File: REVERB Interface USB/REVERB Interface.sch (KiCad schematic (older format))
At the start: 60 parts, among them J1 RPiZeroW, J2 Iridium, J3 APRS, J4 Antenna, J6 USB_B_Micro, J7 USB, J8 USBPOGO, M1 MountingHole_Pad, M2 MountingHole_Pad, M3 MountingHole_Pad, M4 MountingHole_Pad, M5 PiMount, M6 PiMount, M7 PiMount, M8 PiMount, U1 LSM9DS1BOB, U2 MAX3232, U3 CY7C65213-28PVXI, U4 LD1117S33TR_SOT223

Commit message: Remove LDO
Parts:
- removed C10: 0.1uF, Capacitor_SMD:C_0805_2012Metric_Pad1.18x1.45mm_HandSolder, symbol Device:C
- removed C9: 4.7uF, Capacitor_SMD:C_0805_2012Metric_Pad1.18x1.45mm_HandSolder, symbol Device:C
- removed U4: LD1117S33TR_SOT223, Package_TO_SOT_SMD:SOT-223-3_TabPin2, symbol Regulator_Linear:LD1117S33TR_SOT223
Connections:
- net labels removed: SW7STEP3V3
- wire segments 110 -> 102
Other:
- note removed: "5V VCC for 5V USB logic level, 3V3 VCCIO for 3V3 UART output"
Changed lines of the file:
@@
 Text Label 3550 4600 0    50   ~ 0
 D-
-Text Label 2200 4000 0    50   ~ 0
-SW7STEP3V3
 $Comp
 L power:GND #PWR0123
@@
 	1    0    0    -1
 $EndComp
-Text Label 1250 6000 1    50   ~ 0
-SW7
 $Comp
 L power:GND #PWR0127
@@
 	1    0    0    -1
 $EndComp
-Text Label 1450 5200 0    50   ~ 0
-SW7
 Text Label 1450 5400 0    50   ~ 0
 D+
@@
 	3050 4000 3250 4000
 Text Label 3250 4000 0    50   ~ 0
-SW7
-Wire Wire Line
-	1950 6050 2150 6050
-Wire Wire Line
-	2150 6050 2150 6300
-Connection ~ 1950 6050
-Text Label 3200 6300 0    50   ~ 0
-SW7STEP3V3
-Text Notes 850  6950 0    50   ~ 0
-5V VCC for 5V USB logic level, 3V3 VCCIO for 3V3 UART output
+SW10
 Wire Notes Line
 	850  3900 850  6950
@@
 Wire Notes Line
 	3700 3900 3700 6950
-$Comp
-L Regulator_Linear:LD1117S33TR_SOT223 U4
-U 1 1 61636412
-P 2450 6300
-F 0 "U4" H 2450 6542 50  0000 C CNN
-F 1 "LD1117S33TR_SOT223" H 2450 6451 50  0000 C CNN
-F 2 "Package_TO_SOT_SMD:SOT-223-3_TabPin2" H 2450 6500 50  0001 C CNN
-F 3 "http://www.st.com/st-web-ui/static/active/en/resource/technical/document/datasheet/CD00000544.pdf" H 2550 6050 50  0001 C CNN
-	1    2450 6300
-	1    0    0    -1
-$EndComp
-Wire Wire Line
-	1950 6650 2450 6650
-Wire Wire Line
-	2450 6600 2450 6650
-Connection ~ 2450 6650
-$Comp
-L Device:C C10
-U 1 1 616D4D0F
-P 3200 6450
-F 0 "C10" H 3315 6496 50  0000 L CNN
-F 1 "0.1uF" H 3315 6405 50  0000 L CNN
-F 2 "Capacitor_SMD:C_0805_2012Metric_Pad1.18x1.45mm_HandSolder" H 3238 6300 50  0001 C CNN
-F 3 "~" H 3200 6450 50  0001 C CNN
-	1    3200 6450
-	1    0    0    -1
-$EndComp
-$Comp
-L Device:C C9
-U 1 1 616D4D15
-P 2750 6450
-F 0 "C9" H 2865 6496 50  0000 L CNN
-F 1 "4.7uF" H 2865 6405 50  0000 L CNN
-F 2 "Capacitor_SMD:C_0805_2012Metric_Pad1.18x1.45mm_HandSolder" H 2788 6300 50  0001 C CNN
-F 3 "~" H 2750 6450 50  0001 C CNN
-	1    2750 6450
-	1    0    0    -1
-$EndComp
-Wire Wire Line
-	3200 6650 3200 6600
-Wire Wire Line
-	2450 6650 2750 6650
-Wire Wire Line
-	2750 6600 2750 6650
-Connection ~ 2750 6650
-Wire Wire Line
-	2750 6650 3200 6650
-Wire Wire Line
-	2750 6300 3200 6300
 $Comp
 L Device:LED D9
@@
 Wire Wire Line
 	10150 2350 10350 2350
+Wire Wire Line
+	2950 4000 3050 4000
+Connection ~ 2950 4000
+Connection ~ 3050 4000
+Text Label 1250 6000 1    50   ~ 0
+SW10
+Text Label 1450 5200 0    50   ~ 0
+SW10
 $EndSCHEMATC

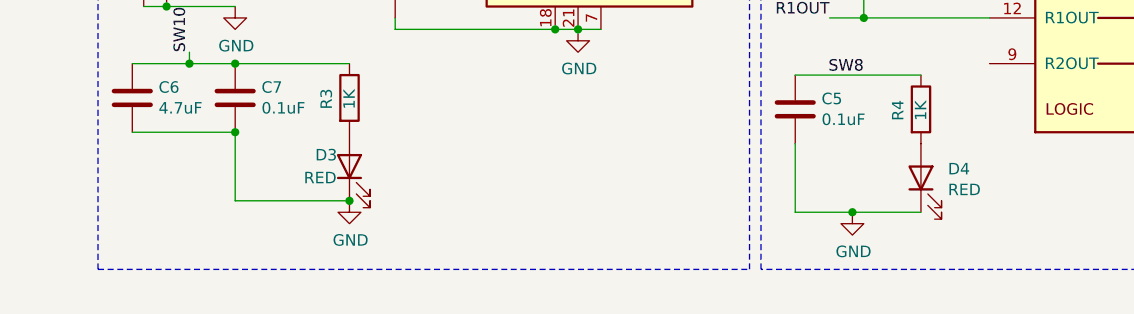
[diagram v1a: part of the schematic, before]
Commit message: Add note regarding usb programming
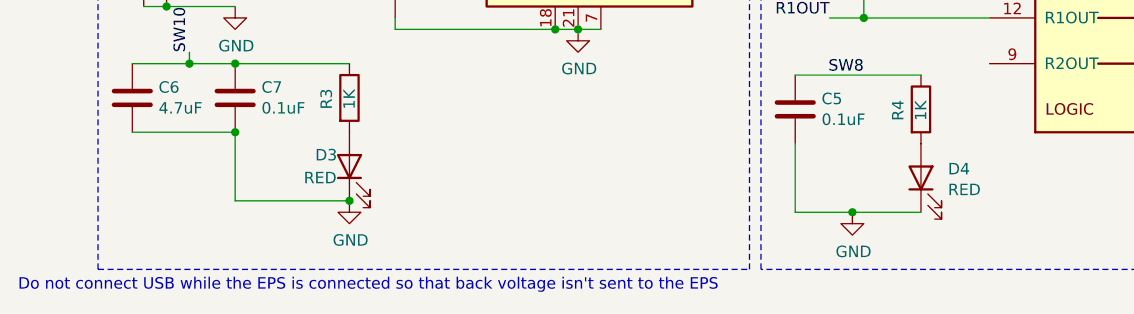
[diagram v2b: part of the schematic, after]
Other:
- note added: "Do not connect USB while the EPS is connected so that back voltage isn't sent to the EPS"
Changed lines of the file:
@@
 Text Label 1450 5200 0    50   ~ 0
 SW10
+Text Notes 500  7050 0    50   ~ 0
+Do not connect USB while the EPS is connected so that back voltage isn't sent to the EPS
 $EndSCHEMATC

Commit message: Replace max3232 footprint, update stencil
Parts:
- U2: footprint REVERB Interface:Texas_Instruments-MAX3232ID -> REVERB Interface:Texas_Instruments-MAX3232ID-Level_A
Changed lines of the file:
@@
 F 0 "U2" H 5550 6731 50  0000 C CNN
 F 1 "MAX3232" H 5550 6640 50  0000 C CNN
-F 2 "REVERB Interface:Texas_Instruments-MAX3232ID" H 5600 4300 50  0001 L CNN
+F 2 "REVERB Interface:Texas_Instruments-MAX3232ID-Level_A" H 5600 4300 50  0001 L CNN
 F 3 "https://datasheets.maximintegrated.com/en/ds/MAX3222-MAX3241.pdf" H 5550 5450 50  0001 C CNN
 	1    5550 5350
@@
 	10350 2350 10750 2350
 $Comp
-L power:GND #PWR?
+L power:GND #PWR0134
 U 1 1 6170EDA2
 P 10150 2350
-F 0 "#PWR?" H 10150 2100 50  0001 C CNN
+F 0 "#PWR0134" H 10150 2100 50  0001 C CNN
 F 1 "GND" H 10155 2177 50  0000 C CNN
 F 2 "" H 10150 2350 50  0001 C CNN

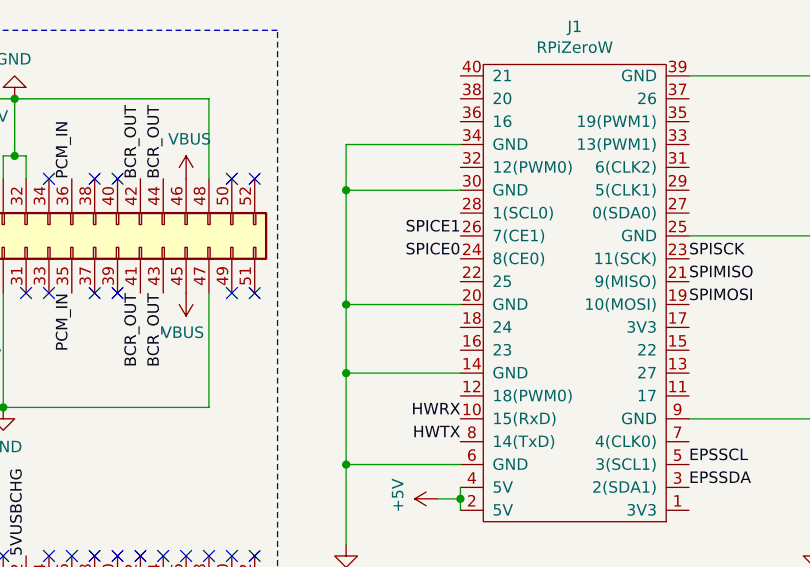
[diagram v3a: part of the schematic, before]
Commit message: Add bitbang uart connections
gpio 23 and 24, #2
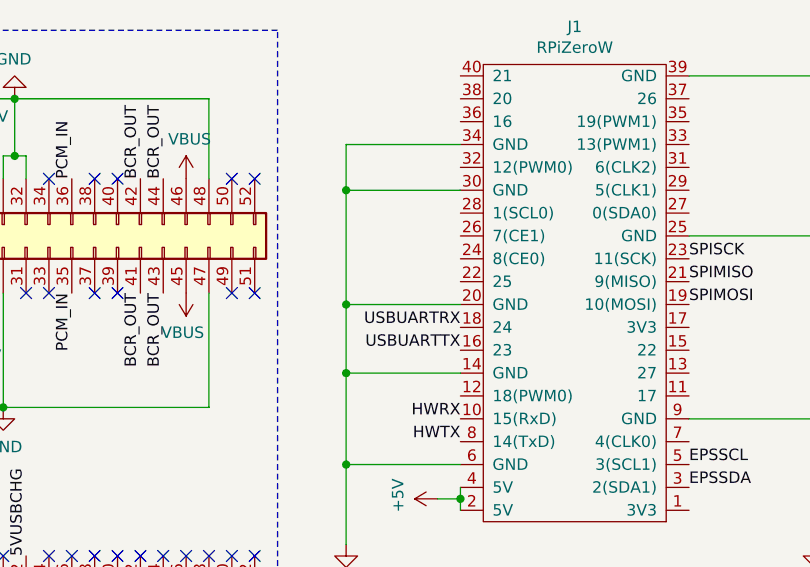
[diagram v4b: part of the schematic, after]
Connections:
- net USBUARTRX: now also J1.18 (24)
- net USBUARTTX: now also J1.16 (23)
- net SPICE0: no longer names the net of J1.24 (8(CE0))
- net SPICE1: no longer names the net of J1.26 (7(CE1))
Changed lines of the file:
@@
 Text Label 6100 1950 0    50   ~ 0
 SPIMOSI
-Text Label 5100 1650 2    50   ~ 0
-SPICE1
-Text Label 5100 1750 2    50   ~ 0
-SPICE0
 $Comp
 L Interface_USB:CY7C65213-28PVXI U3
@@
 Text Notes 500  7050 0    50   ~ 0
 Do not connect USB while the EPS is connected so that back voltage isn't sent to the EPS
+Text Label 5100 2050 2    50   ~ 0
+USBUARTRX
+Text Label 5100 2150 2    50   ~ 0
+USBUARTTX
 $EndSCHEMATC

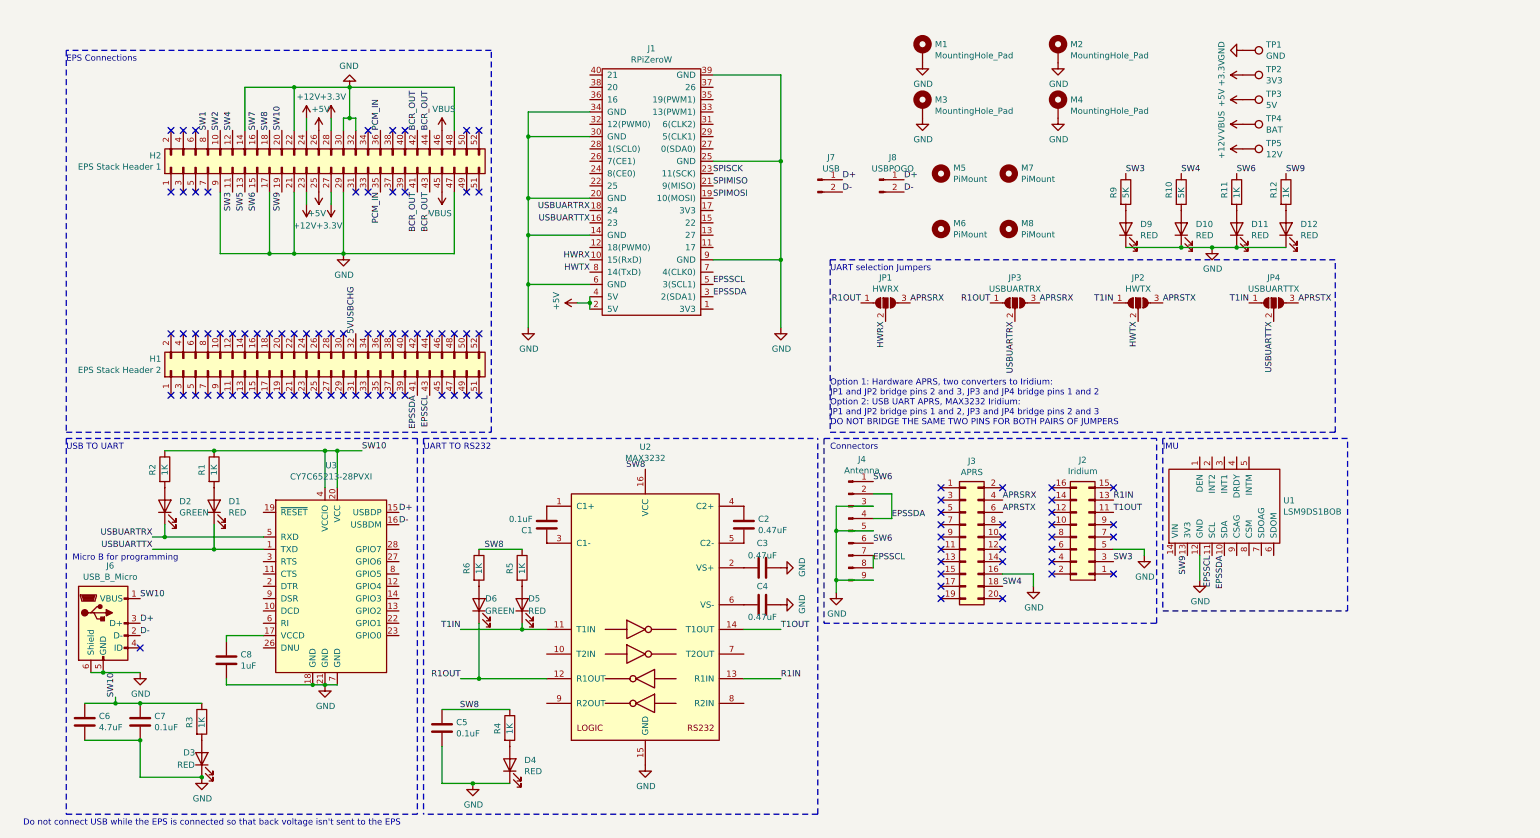
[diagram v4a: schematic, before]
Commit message: Add level shifters, updated sch revision numbers consistent with pcb
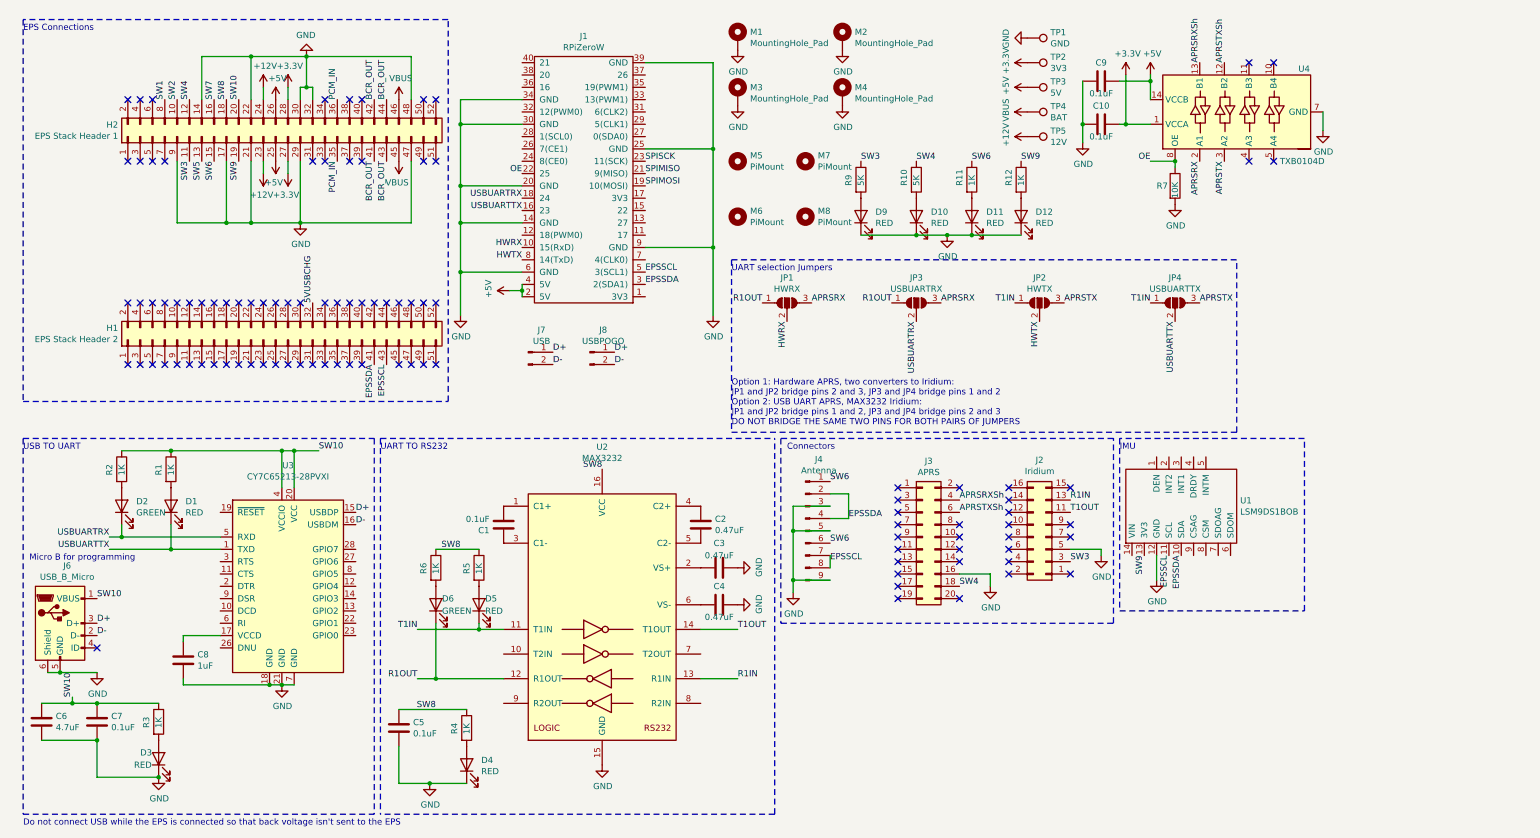
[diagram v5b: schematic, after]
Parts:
- added C10, C9: 0.1uF, Capacitor_SMD:C_0805_2012Metric_Pad1.18x1.45mm_HandSolder, symbol Device:C
- added R7: 10K, Resistor_SMD:R_0805_2012Metric_Pad1.20x1.40mm_HandSolder, symbol Device:R
- added U4: TXB0104D, Package_SO:SOIC-14_3.9x8.7mm_P1.27mm, symbol Logic_LevelTranslator:TXB0104D
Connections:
- net +3V3: now also C10.1, U4.1 (VCCA)
- net +5V: now also C9.1, U4.14 (VCCB)
- net APRSRX: now also U4.2 (A1); no longer J3.4 (Pin_4)
- net APRSTX: now also U4.3 (A2); no longer J3.6 (Pin_6)
- net GND: now also C10.2, C9.2, R7.2, U4.7 (GND)
- net OE: now reaches J1.22 (25)
- net OE: now also R7.1, U4.8 (OE)
- new net APRSRXSh: J3.4 (Pin_4), U4.13 (B1)
- new net APRSTXSh: J3.6 (Pin_6), U4.12 (B2)
- no-connect marks 96 -> 100
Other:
- moved on the sheet: C1, C2, C3, C4, C5, C6, C7, C8, D1, D10, D11, D12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

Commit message: tie OE high
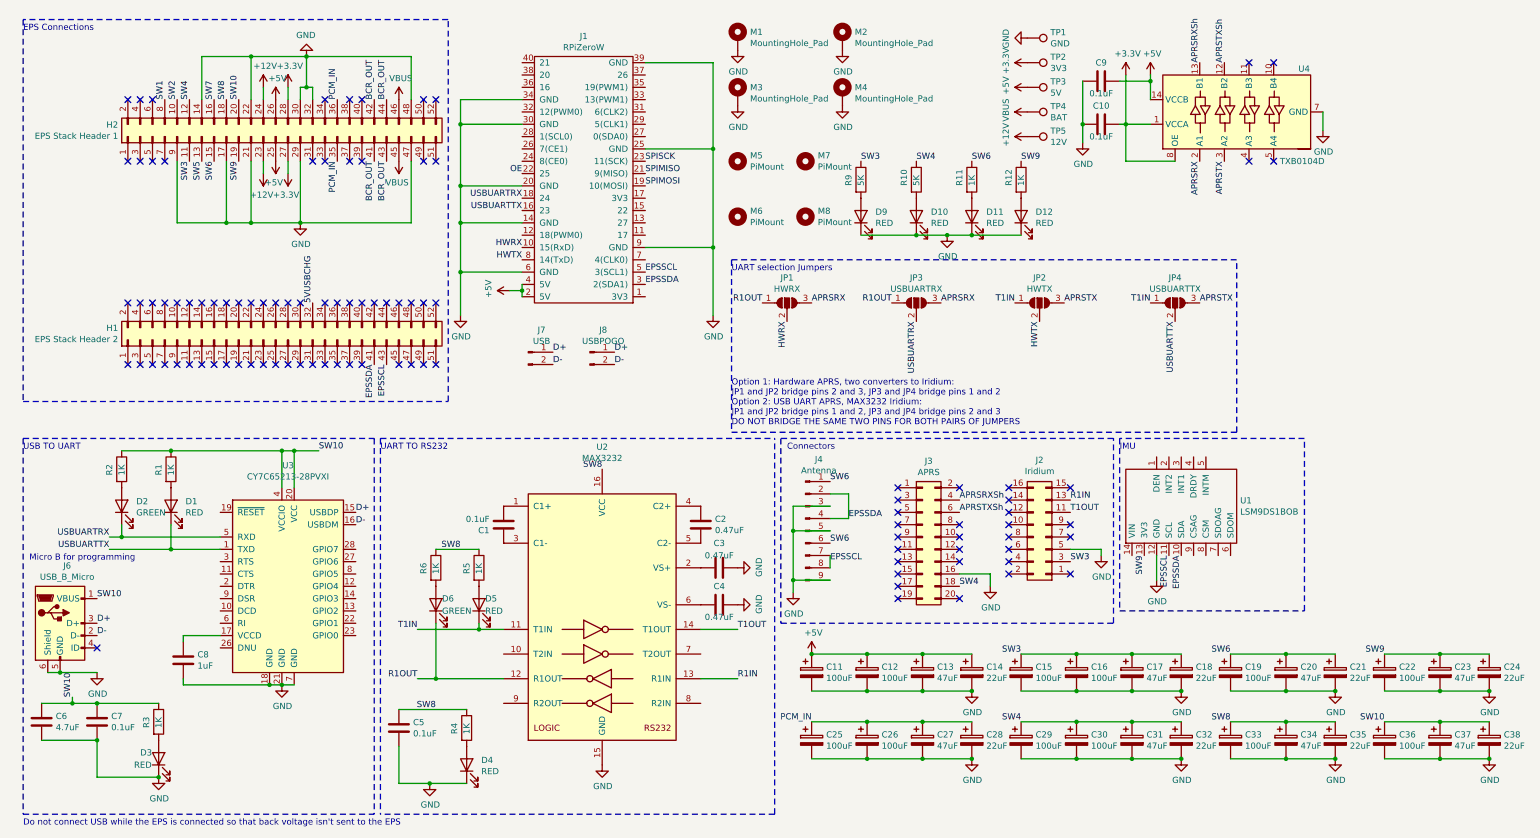
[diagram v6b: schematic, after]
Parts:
- removed R7: 10K, Resistor_SMD:R_0805_2012Metric_Pad1.20x1.40mm_HandSolder, symbol Device:R
- added C11, C12, C15, C16, C19, C22, C25, C26, C29, C30, C33, C36: 100uF, Capacitor_Tantalum_SMD:CP_EIA-7343-43_Kemet-X_Pad2.25x2.55mm_HandSolder, symbol Device:CP
- added C13, C17, C20, C23, C27, C31, C34, C37: 47uF, Capacitor_Tantalum_SMD:CP_EIA-6032-28_Kemet-C_Pad2.25x2.35mm_HandSolder, symbol Device:CP
- added C14, C18, C21, C24, C28, C32, C35, C38: 22uF, Capacitor_Tantalum_SMD:CP_EIA-7343-43_Kemet-X_Pad2.25x2.55mm_HandSolder, symbol Device:CP
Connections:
- net +3V3: now also U4.8 (OE)
- net +5V: now also C11.1, C12.1, C13.1, C14.1
- net GND: now also C11.2, C12.2, C13.2, C14.2, C15.2, C16.2, C17.2, C18.2, C19.2, C20.2, C21.2, C22.2, C23.2, C24.2, C25.2, C26.2, C27.2, C28.2, C29.2, C30.2, C31.2, C32.2, C33.2, C34.2, C35.2, C36.2, C37.2, C38.2
- net OE: no longer U4.8 (OE)
- net PCM_IN: now also C25.1, C26.1, C27.1, C28.1
- net SW10: now also C36.1, C37.1, C38.1
- net SW3: now also C15.1, C16.1, C17.1, C18.1
- net SW4: now also C29.1, C30.1, C31.1, C32.1
- net SW6: now also C19.1, C20.1, C21.1
- net SW8: now also C33.1, C34.1, C35.1
- net SW9: now also C22.1, C23.1, C24.1
